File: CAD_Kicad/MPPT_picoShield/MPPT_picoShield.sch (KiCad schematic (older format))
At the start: 61 parts, among them J1 PV_input, J2 Battery_pack, J3 V_out, J4 Micro_SD_Card_Det_Hirose_DM3AT, J5 GPIO breakout, Q1 PMOS_GDS_TO220, Q2 NMOS_DGS_SOT23, Q3 NMOS_DGS_SOT23, SW1 RESET, U1 RaspiPico, U10 LF50_TO220, U2 INA3221

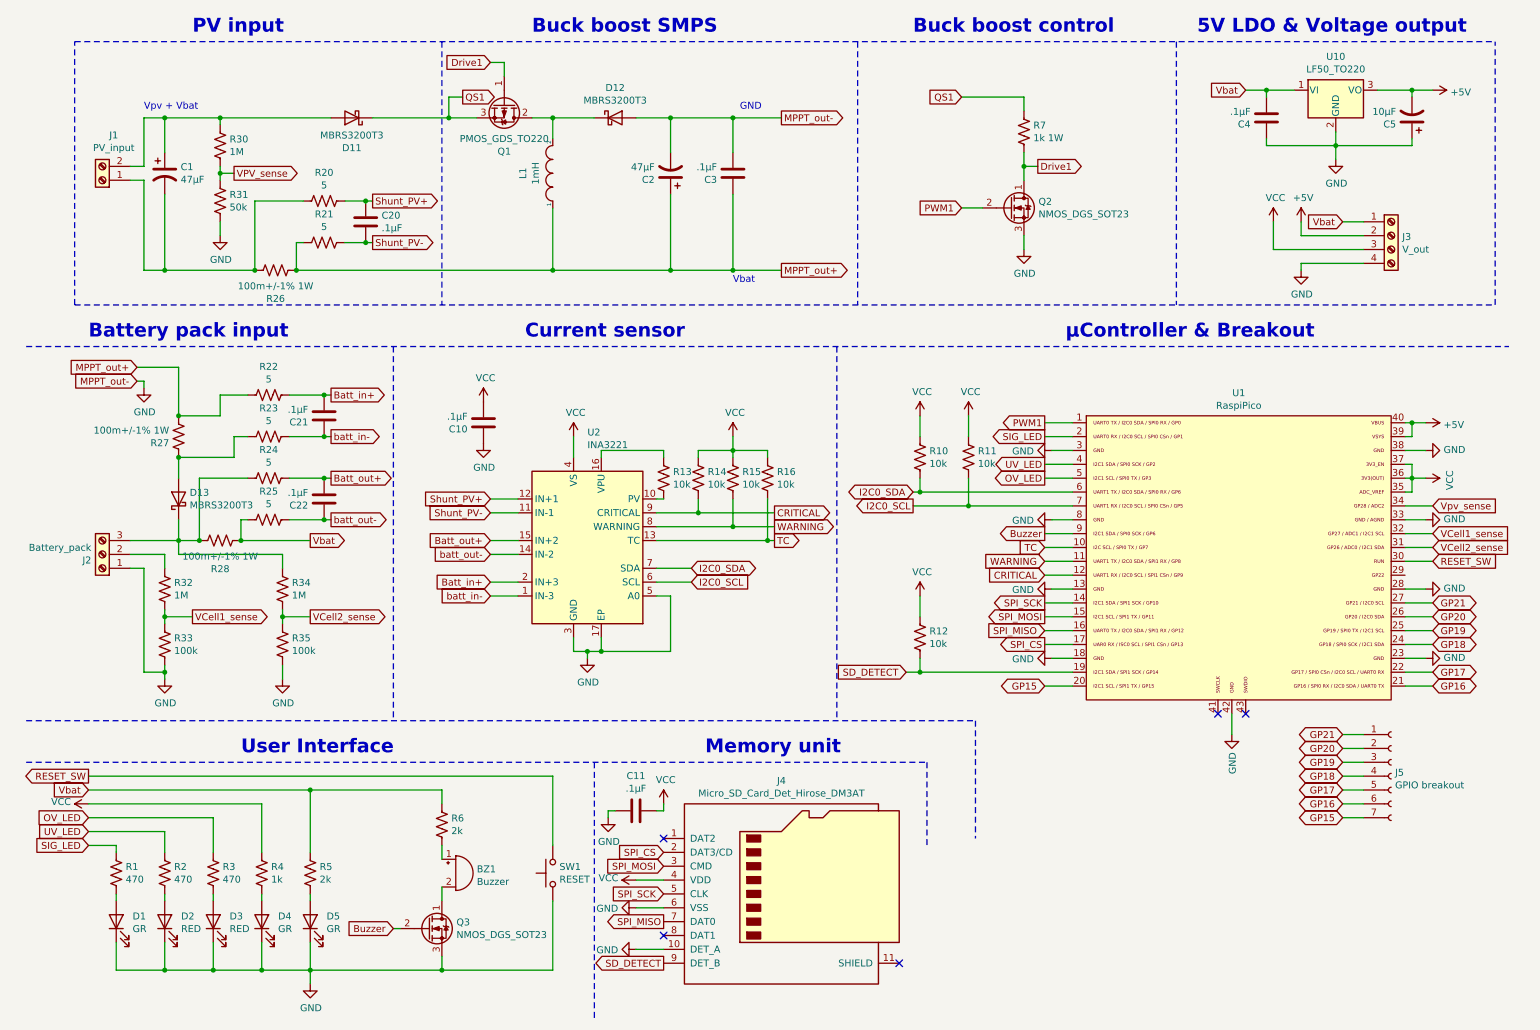
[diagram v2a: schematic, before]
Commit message: Initial routing
Small verifications to be made: 
- Should Metal of INA2331 be connected to ground? Or a floating metal plane? or Vcc?
- Should capacitors be added to the long analog lines to stabilize them?
- Should D11 and its polarized cap be swapped to "idiot proof" the PV connector?
- Rasp Pico silkscreen is outside of PCB, should probably fix that
- Indicator of pin 1 on INA2331 is overlapping a via, small esthetic fix to be made
- Note for future: DPAK or TO220?
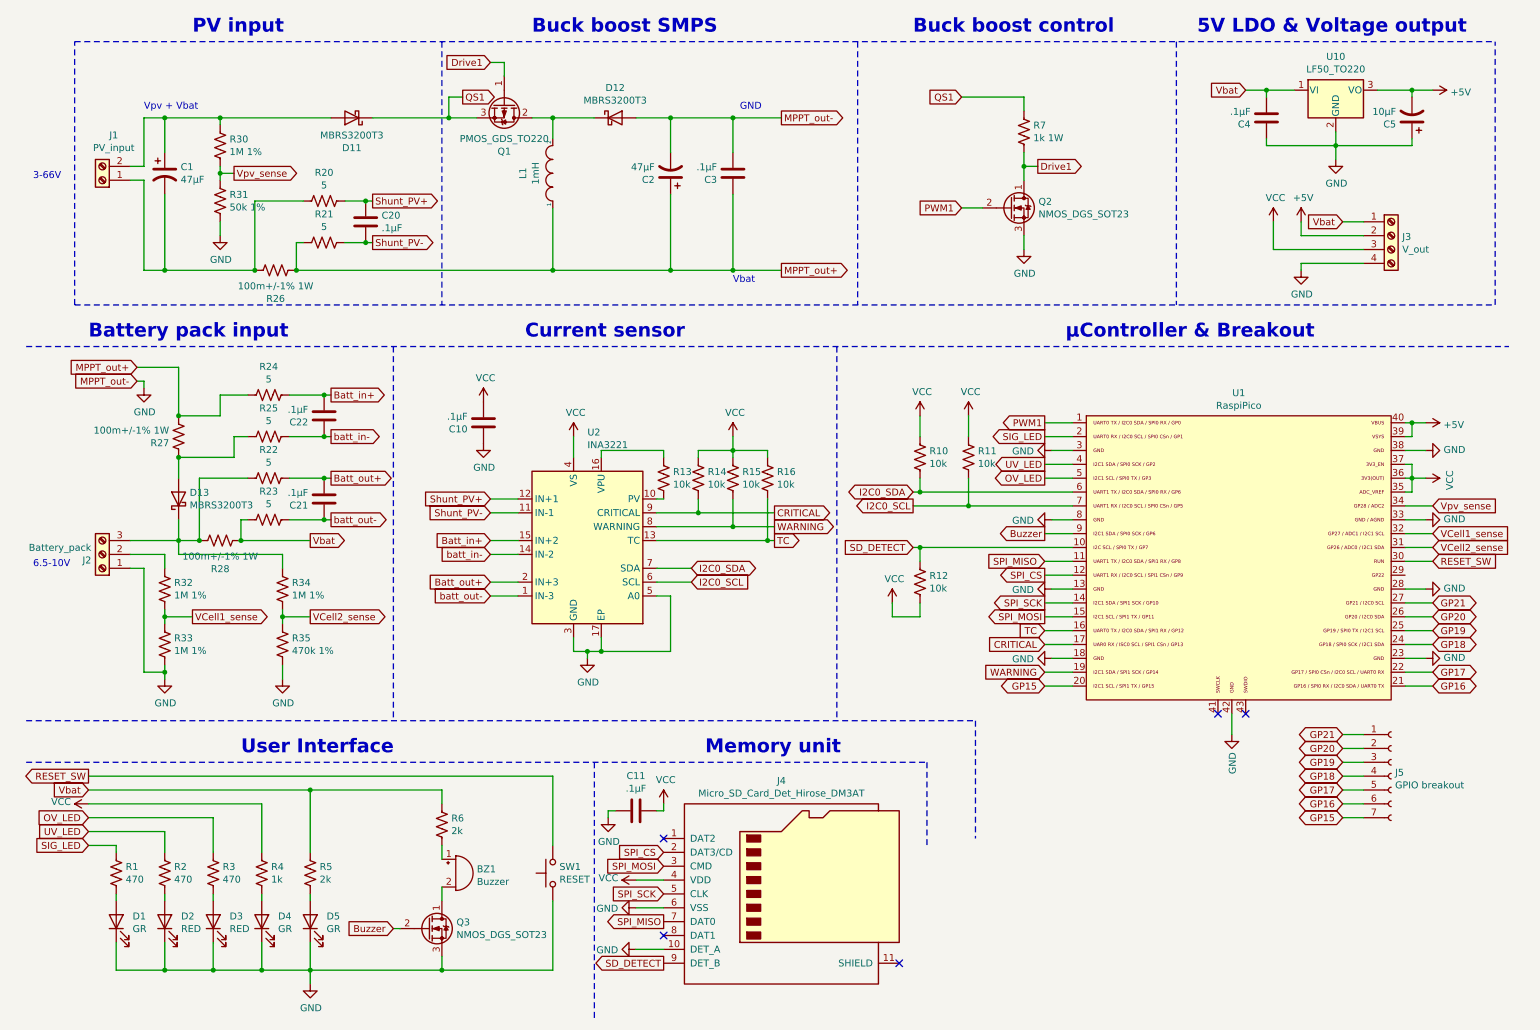
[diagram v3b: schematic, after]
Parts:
- R30, R32, R34: value 1M -> 1M 1%
- R31: value 50k -> 50k 1%
- R33: value 100k -> 1M 1%
- R35: value 100k -> 470k 1%
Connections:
- net VPV_sense is gone; now on net Vpv_sense: R30.2, R31.1
- net Batt_in+: now also C22.2, R24.1, U2.15 (IN+2); no longer C21.2, R22.1, U2.2 (IN+3)
- net Batt_out+: now also C21.2, R22.1, U2.2 (IN+3); no longer C22.2, R24.1, U2.15 (IN+2)
- net CRITICAL: now also U1.17; no longer U1.12
- net MPPT_out+: now also R24.2; no longer R22.2
- net SD_DETECT: now also R12.1, U1.10; no longer R12.2, U1.19
- net SPI_CS: now also U1.12; no longer U1.17
- net SPI_MISO: now also U1.11; no longer U1.16
- net TC: now also U1.16; no longer U1.10
- net VCC: now also R12.2; no longer R12.1
- net Vbat: now also R23.2; no longer R25.2
- net WARNING: now also U1.19; no longer U1.11
- net batt_in-: now also C22.1, R25.1, U2.14 (IN-2); no longer C21.1, R23.1, U2.1 (IN-3)
- net batt_out-: now also C21.1, R23.1, U2.1 (IN-3); no longer C22.1, R25.1, U2.14 (IN-2)
- net at D13.2 (A), R27.1: now also R25.2; no longer R23.2
- net at D13.1 (K), J2.3 (Pin_3), R28.1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: now also R22.2; no longer R24.2
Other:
- note added: "3-66V"
- note added: "6.5-10V"
- moved on the sheet: C21, C22, R12, R22, R23, R24, R25
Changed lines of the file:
@@
 P 1900 1500
 F 0 "R30" H 1968 1546 50  0000 L CNN
-F 1 "1M" H 1968 1455 50  0000 L CNN
+F 1 "1M 1%" H 1968 1455 50  0000 L CNN
 F 2 "Resistor_SMD:R_0603_1608Metric" V 1940 1490 50  0001 C CNN
 F 3 "~" H 1900 1500 50  0001 C CNN
@@
 P 1900 1900
 F 0 "R31" H 1968 1946 50  0000 L CNN
-F 1 "50k" H 1968 1855 50  0000 L CNN
+F 1 "50k 1%" H 1968 1855 50  0000 L CNN
 F 2 "Resistor_SMD:R_0603_1608Metric" V 1940 1890 50  0001 C CNN
 F 3 "~" H 1900 1900 50  0001 C CNN
@@
 Wire Wire Line
 	3850 900  3950 900
-Text GLabel 3000 1900 2    50   Output ~ 0
-Shunt_PV+
-Text GLabel 3000 2200 2    50   Output ~ 0
-Shunt_PV-
 Text GLabel 2000 1700 2    50   Output ~ 0
-VPV_sense
+Vpv_sense
 Text GLabel 5950 2400 2    50   Output ~ 0
 MPPT_out+
@@
 P 1500 4700
 F 0 "R32" H 1568 4746 50  0000 L CNN
-F 1 "1M" H 1568 4655 50  0000 L CNN
+F 1 "1M 1%" H 1568 4655 50  0000 L CNN
 F 2 "Resistor_SMD:R_0603_1608Metric" V 1540 4690 50  0001 C CNN
 F 3 "~" H 1500 4700 50  0001 C CNN
@@
 P 1500 5100
 F 0 "R33" H 1568 5146 50  0000 L CNN
-F 1 "100k" H 1568 5055 50  0000 L CNN
+F 1 "1M 1%" H 1568 5055 50  0000 L CNN
 F 2 "Resistor_SMD:R_0603_1608Metric" V 1540 5090 50  0001 C CNN
 F 3 "~" H 1500 5100 50  0001 C CNN
@@
 P 2350 4700
 F 0 "R34" H 2418 4746 50  0000 L CNN
-F 1 "1M" H 2418 4655 50  0000 L CNN
+F 1 "1M 1%" H 2418 4655 50  0000 L CNN
 F 2 "Resistor_SMD:R_0603_1608Metric" V 2390 4690 50  0001 C CNN
 F 3 "~" H 2350 4700 50  0001 C CNN
@@
 P 2350 5100
 F 0 "R35" H 2418 5146 50  0000 L CNN
-F 1 "100k" H 2418 5055 50  0000 L CNN
+F 1 "470k 1%" H 2418 5055 50  0000 L CNN
 F 2 "Resistor_SMD:R_0603_1608Metric" V 2390 5090 50  0001 C CNN
 F 3 "~" H 2350 5100 50  0001 C CNN
@@
 	1    0    0    -1
 $EndComp
-$Comp
-L Connector:Screw_Terminal_01x04 J3
-U 1 1 62841410
-P 10350 2150
-F 0 "J3" H 10430 2142 50  0000 L CNN
-F 1 "V_out" H 10430 2051 50  0000 L CNN
-F 2 "TerminalBlock:TerminalBlock_bornier-4_P5.08mm" H 10350 2150 50  0001 C CNN
-F 3 "~" H 10350 2150 50  0001 C CNN
-	1    10350 2150
-	1    0    0    -1
-$EndComp
 Text GLabel 10000 2050 0    50   Input ~ 0
 Vbat
@@
 Wire Notes Line
 	3150 2950 3150 5650
-Text GLabel 6850 5300 0    50   Input ~ 0
+Text GLabel 6900 4400 0    50   Input ~ 0
 SD_DETECT
 Wire Wire Line
@@
 Wire Wire Line
 	4050 4050 3850 4050
-Text GLabel 3850 4450 0    50   Input ~ 0
+Text GLabel 3850 4750 0    50   Input ~ 0
 batt_out-
-Text GLabel 3850 4350 0    50   Input ~ 0
+Text GLabel 3850 4650 0    50   Input ~ 0
 Batt_out+
 Text GLabel 3850 4150 0    50   Input ~ 0
@@
 Text GLabel 3850 4050 0    50   Input ~ 0
 Shunt_PV+
-Text GLabel 3850 4750 0    50   Input ~ 0
+Text GLabel 3850 4450 0    50   Input ~ 0
 batt_in-
-Text GLabel 3850 4650 0    50   Input ~ 0
+Text GLabel 3850 4350 0    50   Input ~ 0
 Batt_in+
 Text GLabel 6900 4000 0    50   BiDi ~ 0
@@
 Text Notes 4100 2900 0    100  ~ 20
 Current sensor
-Text GLabel 7850 4600 0    50   Input ~ 0
+Text GLabel 7850 5100 0    50   Input ~ 0
 CRITICAL
-Text GLabel 7850 4500 0    50   Input ~ 0
+Text GLabel 7850 5300 0    50   Input ~ 0
 WARNING
-Text GLabel 7850 4400 0    50   Input ~ 0
+Text GLabel 7850 5000 0    50   Input ~ 0
 TC
-Wire Wire Line
-	8050 4400 7850 4400
 Wire Wire Line
 	8050 4500 7850 4500
@@
 Text GLabel 7850 4900 0    50   Output ~ 0
 SPI_MOSI
-Text GLabel 7850 5000 0    50   Input ~ 0
+Text GLabel 7850 4500 0    50   Input ~ 0
 SPI_MISO
-Text GLabel 7850 5100 0    50   Output ~ 0
+Text GLabel 7850 4600 0    50   Output ~ 0
 SPI_CS
 Wire Wire Line
@@
 L Device:R_US R12
 U 1 1 62A3F116
-P 6950 5050
-F 0 "R12" H 7018 5096 50  0000 L CNN
-F 1 "10k" H 7018 5005 50  0000 L CNN
-F 2 "Resistor_SMD:R_0603_1608Metric" V 6990 5040 50  0001 C CNN
-F 3 "~" H 6950 5050 50  0001 C CNN
-	1    6950 5050
-	1    0    0    -1
-$EndComp
-Wire Wire Line
-	6950 4900 6950 4750
+P 6950 4650
+F 0 "R12" H 7018 4696 50  0000 L CNN
+F 1 "10k" H 7018 4605 50  0000 L CNN
+F 2 "Resistor_SMD:R_0603_1608Metric" V 6990 4640 50  0001 C CNN
+F 3 "~" H 6950 4650 50  0001 C CNN
+	1    6950 4650
+	1    0    0    -1
+$EndComp
 $Comp
 L power:VCC #PWR0135
 U 1 1 62AA6FD9
-P 6950 4750
-F 0 "#PWR0135" H 6950 4600 50  0001 C CNN
-F 1 "VCC" H 6965 4923 50  0000 C CNN
-F 2 "" H 6950 4750 50  0001 C CNN
-F 3 "" H 6950 4750 50  0001 C CNN
-	1    6950 4750
-	1    0    0    -1
-$EndComp
-Wire Wire Line
-	6850 5300 6950 5300
-Wire Wire Line
-	6950 5300 6950 5200
-Wire Wire Line
-	6950 5300 8050 5300
-Connection ~ 6950 5300
+P 6750 4800
+F 0 "#PWR0135" H 6750 4650 50  0001 C CNN
+F 1 "VCC" H 6765 4973 50  0000 C CNN
+F 2 "" H 6750 4800 50  0001 C CNN
+F 3 "" H 6750 4800 50  0001 C CNN
+	1    6750 4800
+	1    0    0    -1
+$EndComp
 NoConn ~ 9100 5600
 NoConn ~ 9300 5600
@@
 L Device:R_US R24
 U 1 1 62CD965F
+P 2250 3300
+F 0 "R24" V 2045 3300 50  0000 C CNN
+F 1 "5" V 2136 3300 50  0000 C CNN
+F 2 "Resistor_SMD:R_0603_1608Metric" V 2290 3290 50  0001 C CNN
+F 3 "~" H 2250 3300 50  0001 C CNN
+	1    2250 3300
+	0    1    1    0
+$EndComp
+$Comp
+L Device:R_US R25
+U 1 1 62CDA8DB
+P 2250 3600
+F 0 "R25" V 2045 3600 50  0000 C CNN
+F 1 "5" V 2136 3600 50  0000 C CNN
+F 2 "Resistor_SMD:R_0603_1608Metric" V 2290 3590 50  0001 C CNN
+F 3 "~" H 2250 3600 50  0001 C CNN
+	1    2250 3600
+	0    1    1    0
+$EndComp
+$Comp
+L Device:C C22
+U 1 1 62CEA140
+P 2650 3450
+F 0 "C22" H 2765 3496 50  0000 L CNN
+F 1 ".1µF" H 2765 3405 50  0000 L CNN
+F 2 "Capacitor_SMD:C_0603_1608Metric" H 2688 3300 50  0001 C CNN
+F 3 "~" H 2650 3450 50  0001 C CNN
+	1    2650 3450
+	-1   0    0    1
+$EndComp
+$Comp
+L Device:R_US R22
+U 1 1 62DBDC5D
 P 2250 3900
-F 0 "R24" V 2045 3900 50  0000 C CNN
+F 0 "R22" V 2045 3900 50  0000 C CNN
 F 1 "5" V 2136 3900 50  0000 C CNN
 F 2 "Resistor_SMD:R_0603_1608Metric" V 2290 3890 50  0001 C CNN
@@
 $EndComp
 $Comp
-L Device:R_US R25
-U 1 1 62CDA8DB
+L Device:R_US R23
+U 1 1 62DBDC63
 P 2250 4200
-F 0 "R25" V 2045 4200 50  0000 C CNN
+F 0 "R23" V 2045 4200 50  0000 C CNN
 F 1 "5" V 2136 4200 50  0000 C CNN
 F 2 "Resistor_SMD:R_0603_1608Metric" V 2290 4190 50  0001 C CNN
@@
 $EndComp
 $Comp
-L Device:C C22
-U 1 1 62CEA140
+L Device:C C21
+U 1 1 62E1B00F
 P 2650 4050
-F 0 "C22" H 2765 4096 50  0000 L CNN
+F 0 "C21" H 2765 4096 50  0000 L CNN
 F 1 ".1µF" H 2765 4005 50  0000 L CNN
 F 2 "Capacitor_SMD:C_0603_1608Metric" H 2688 3900 50  0001 C CNN
@@
 	-1   0    0    1
 $EndComp
-$Comp
-L Device:R_US R22
-U 1 1 62DBDC5D
-P 2250 3300
-F 0 "R22" V 2045 3300 50  0000 C CNN
-F 1 "5" V 2136 3300 50  0000 C CNN
-F 2 "Resistor_SMD:R_0603_1608Metric" V 2290 3290 50  0001 C CNN
-F 3 "~" H 2250 3300 50  0001 C CNN
-	1    2250 3300
-	0    1    1    0
-$EndComp
-$Comp
-L Device:R_US R23
-U 1 1 62DBDC63
-P 2250 3600
-F 0 "R23" V 2045 3600 50  0000 C CNN
-F 1 "5" V 2136 3600 50  0000 C CNN
-F 2 "Resistor_SMD:R_0603_1608Metric" V 2290 3590 50  0001 C CNN
-F 3 "~" H 2250 3600 50  0001 C CNN
-	1    2250 3600
-	0    1    1    0
-$EndComp
-$Comp
-L Device:C C21
-U 1 1 62E1B00F
-P 2650 3450
-F 0 "C21" H 2765 3496 50  0000 L CNN
-F 1 ".1µF" H 2765 3405 50  0000 L CNN
-F 2 "Capacitor_SMD:C_0603_1608Metric" H 2688 3300 50  0001 C CNN
-F 3 "~" H 2650 3450 50  0001 C CNN
-	1    2650 3450
-	-1   0    0    1
-$EndComp
 Wire Wire Line
 	2100 3600 2000 3600
@@
 	1900 3300 2100 3300
 Wire Wire Line
-	2700 3300 2650 3300
+	2700 3900 2650 3900
 $Comp
 L Device:R_US R20
@@
 Wire Wire Line
 	2950 2200 3000 2200
+Connection ~ 2650 3300
+Wire Wire Line
+	2650 3300 2700 3300
+Connection ~ 2650 3600
+Wire Wire Line
+	2650 3600 2700 3600
+Wire Wire Line
+	2400 3600 2650 3600
+Wire Wire Line
+	2400 3300 2650 3300
 Connection ~ 2650 3900
-Wire Wire Line
-	2650 3900 2700 3900
 Connection ~ 2650 4200
 Wire Wire Line
@@
 Wire Wire Line
 	2400 3900 2650 3900
-Connection ~ 2650 3300
-Connection ~ 2650 3600
-Wire Wire Line
-	2650 3600 2700 3600
-Wire Wire Line
-	2400 3600 2650 3600
-Wire Wire Line
-	2400 3300 2650 3300
 $Comp
 L Connector:Micro_SD_Card_Det_Hirose_DM3AT J4
@@
 Wire Wire Line
 	1250 4350 1600 4350
+Text GLabel 3000 2200 2    50   Output ~ 0
+Shunt_PV-
+Text GLabel 3000 1900 2    50   Output ~ 0
+Shunt_PV+
+Text Notes 550  1750 0    50   ~ 0
+3-66V
+Text Notes 550  4550 0    50   ~ 0
+6.5-10V
+Wire Wire Line
+	7850 5300 8050 5300
+Wire Wire Line
+	6950 4500 6950 4400
+Wire Wire Line
+	6950 4400 8050 4400
+Wire Wire Line
+	6950 4800 6950 4900
+Wire Wire Line
+	6750 4900 6950 4900
+Wire Wire Line
+	6750 4900 6750 4800
+Wire Wire Line
+	6950 4400 6900 4400
+Connection ~ 6950 4400
+$Comp
+L Connector:Screw_Terminal_01x04 J3
+U 1 1 62841410
+P 10350 2150
+F 0 "J3" H 10430 2142 50  0000 L CNN
+F 1 "V_out" H 10430 2051 50  0000 L CNN
+F 2 "TerminalBlock:TerminalBlock_bornier-4_P5.08mm" H 10350 2150 50  0001 C CNN
+F 3 "~" H 10350 2150 50  0001 C CNN
+	1    10350 2150
+	1    0    0    -1
+$EndComp
 $EndSCHEMATC

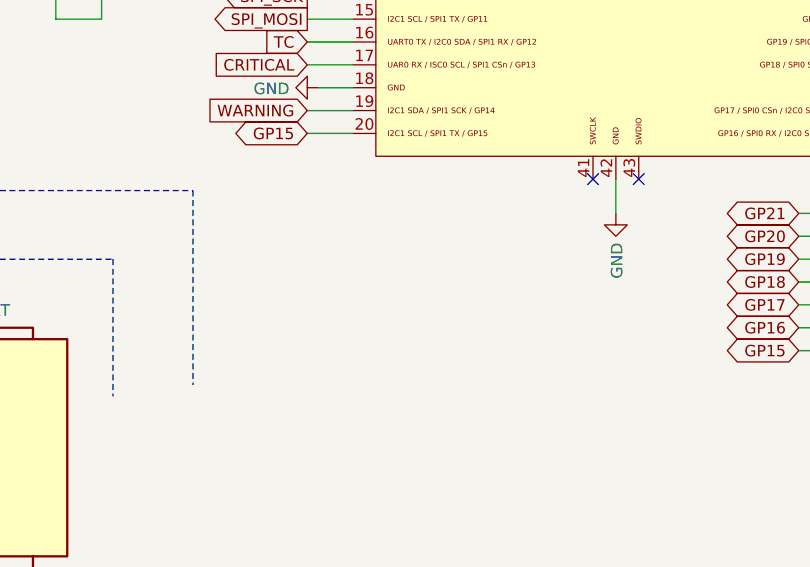
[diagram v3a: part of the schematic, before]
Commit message: Gerber gen and added filtering caps on ADC lines
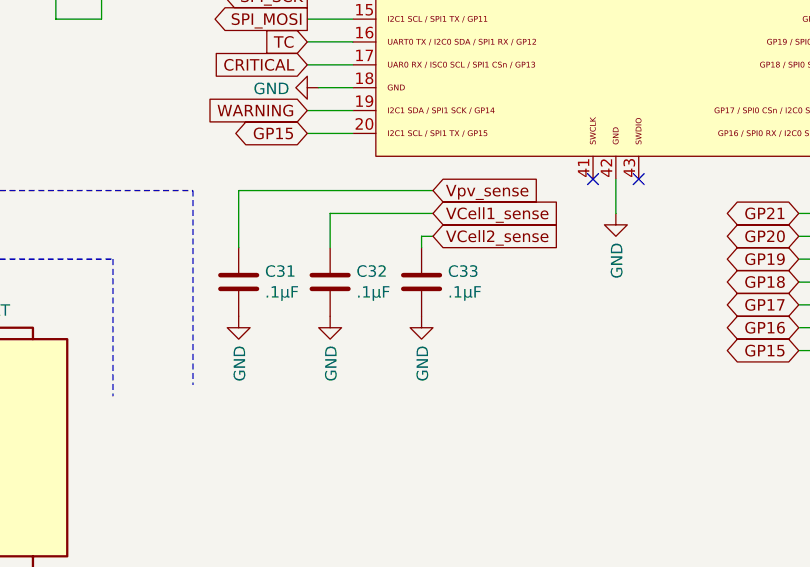
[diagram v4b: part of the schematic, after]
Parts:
- added C31, C32, C33: .1µF, Capacitor_SMD:C_0603_1608Metric, symbol Device:C
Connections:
- net GND: now also C31.2, C32.2, C33.2
- net VCell1_sense: now also C32.1
- net VCell2_sense: now also C33.1
- net Vpv_sense: now also C31.1
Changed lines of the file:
@@
 	1    0    0    -1
 $EndComp
+Text GLabel 8400 5850 2    50   Input ~ 0
+VCell2_sense
+Text GLabel 8400 5750 2    50   Input ~ 0
+VCell1_sense
+Text GLabel 8400 5650 2    50   Input ~ 0
+Vpv_sense
+$Comp
+L Device:C C31
+U 1 1 6240649C
+P 7550 6050
+F 0 "C31" H 7665 6096 50  0000 L CNN
+F 1 ".1µF" H 7665 6005 50  0000 L CNN
+F 2 "Capacitor_SMD:C_0603_1608Metric" H 7588 5900 50  0001 C CNN
+F 3 "~" H 7550 6050 50  0001 C CNN
+	1    7550 6050
+	1    0    0    -1
+$EndComp
+$Comp
+L Device:C C32
+U 1 1 624198D1
+P 7950 6050
+F 0 "C32" H 8065 6096 50  0000 L CNN
+F 1 ".1µF" H 8065 6005 50  0000 L CNN
+F 2 "Capacitor_SMD:C_0603_1608Metric" H 7988 5900 50  0001 C CNN
+F 3 "~" H 7950 6050 50  0001 C CNN
+	1    7950 6050
+	1    0    0    -1
+$EndComp
+$Comp
+L Device:C C33
+U 1 1 6242CB53
+P 8350 6050
+F 0 "C33" H 8465 6096 50  0000 L CNN
+F 1 ".1µF" H 8465 6005 50  0000 L CNN
+F 2 "Capacitor_SMD:C_0603_1608Metric" H 8388 5900 50  0001 C CNN
+F 3 "~" H 8350 6050 50  0001 C CNN
+	1    8350 6050
+	1    0    0    -1
+$EndComp
+$Comp
+L power:GND #PWR?
+U 1 1 6247B261
+P 7550 6200
+F 0 "#PWR?" H 7550 5950 50  0001 C CNN
+F 1 "GND" V 7555 6072 50  0000 R CNN
+F 2 "" H 7550 6200 50  0001 C CNN
+F 3 "" H 7550 6200 50  0001 C CNN
+	1    7550 6200
+	1    0    0    -1
+$EndComp
+$Comp
+L power:GND #PWR?
+U 1 1 6248E4CC
+P 7950 6200
+F 0 "#PWR?" H 7950 5950 50  0001 C CNN
+F 1 "GND" V 7955 6072 50  0000 R CNN
+F 2 "" H 7950 6200 50  0001 C CNN
+F 3 "" H 7950 6200 50  0001 C CNN
+	1    7950 6200
+	1    0    0    -1
+$EndComp
+$Comp
+L power:GND #PWR?
+U 1 1 624A16F1
+P 8350 6200
+F 0 "#PWR?" H 8350 5950 50  0001 C CNN
+F 1 "GND" V 8355 6072 50  0000 R CNN
+F 2 "" H 8350 6200 50  0001 C CNN
+F 3 "" H 8350 6200 50  0001 C CNN
+	1    8350 6200
+	1    0    0    -1
+$EndComp
+Wire Wire Line
+	8350 5900 8350 5850
+Wire Wire Line
+	8350 5850 8400 5850
+Wire Wire Line
+	7950 5750 7950 5900
+Wire Wire Line
+	7950 5750 8400 5750
+Wire Wire Line
+	8400 5650 7550 5650
+Wire Wire Line
+	7550 5650 7550 5900
 $EndSCHEMATC
